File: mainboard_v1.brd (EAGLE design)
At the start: 100 x 50 mm, 16 parts

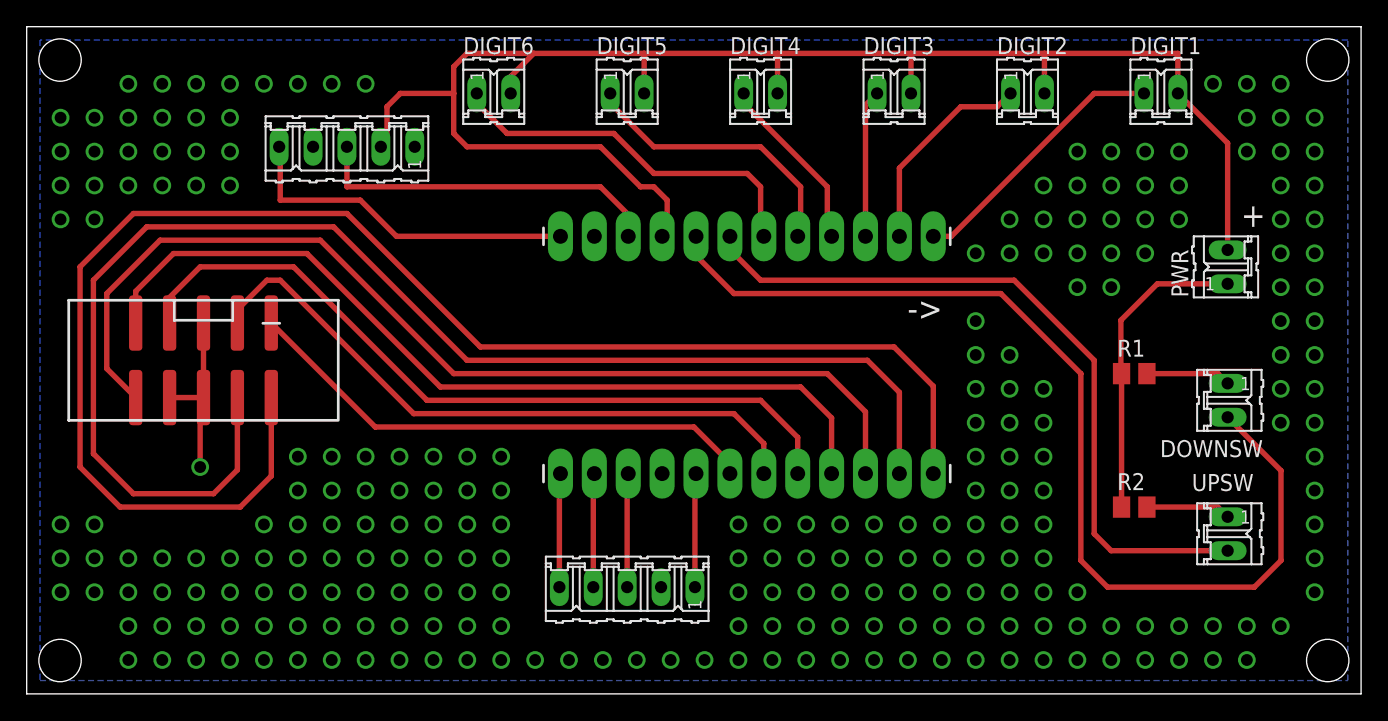
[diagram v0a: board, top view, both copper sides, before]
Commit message: add labels to boards to aid in, you know, using them
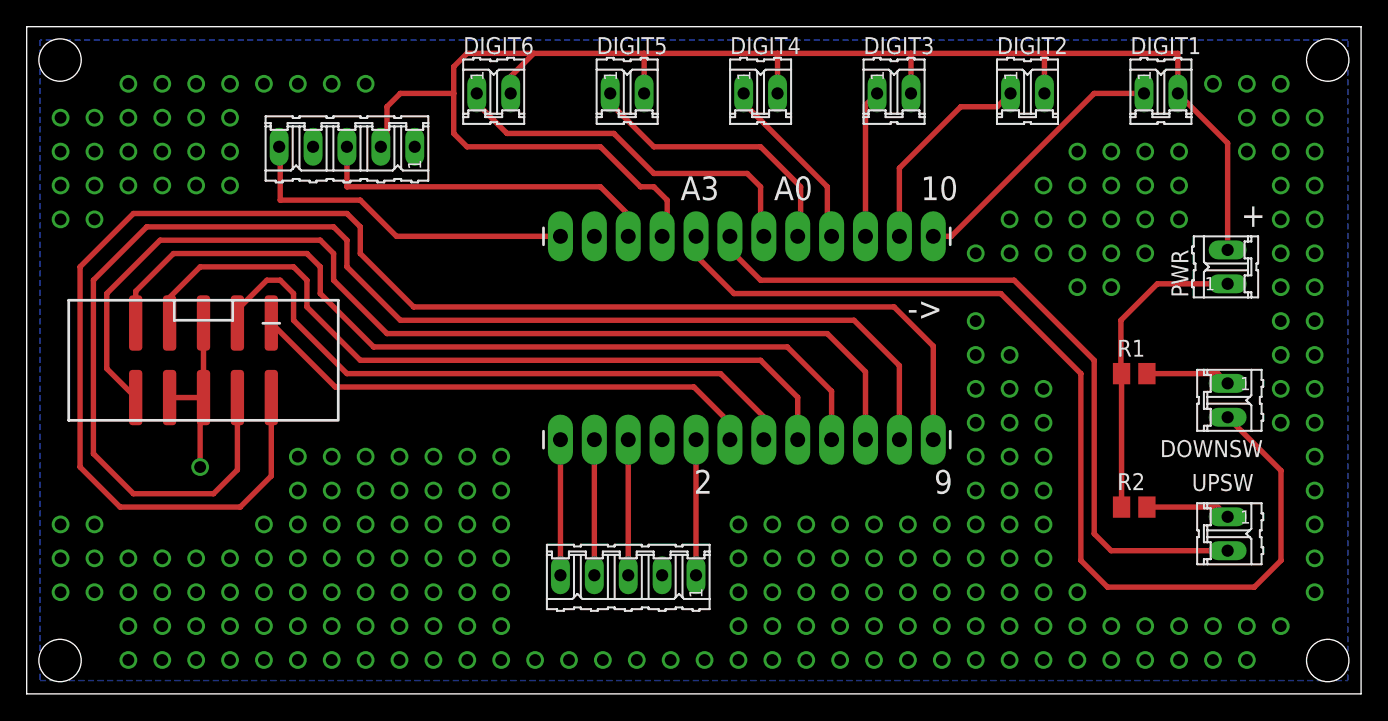
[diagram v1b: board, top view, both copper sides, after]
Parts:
- moved HDRRIGHT 2.54 mm to (40.0, 19.1)
- moved BREAKOUT 0.89 mm to (45.1, 8.89)
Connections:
- net CATH1 renamed SEG_A
- net CATH2 renamed SEG_B
- net CATH3 renamed SEG_F
- net CATH4 renamed SEG_G
- net CATH5 renamed SEG_C
- net CATH6 renamed SEG_E
- net CATH7 renamed SEG_D
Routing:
- net N$7: track 8.54 -> 10.2 mm
- net N$6: track 8.54 -> 10.2 mm
- net N$5: track 8.54 -> 10.2 mm
- net N$2: track 8.54 -> 10.2 mm
- net SEG_F: track 39.5 -> 38.7 mm
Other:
- board text added: "10"
- board text added: "2"
- board text added: "9"
- board text added: "A0"
- board text added: "A3"
